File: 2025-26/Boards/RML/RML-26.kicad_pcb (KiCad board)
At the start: 2 copper layers, 90.1 x 30 mm, 26 parts, among them J1 043045-0412, Q2 AO3401A, Q3 UJ3N065080K3S, Q4 AO3401A, U1 H11L1M, U2 NE555D

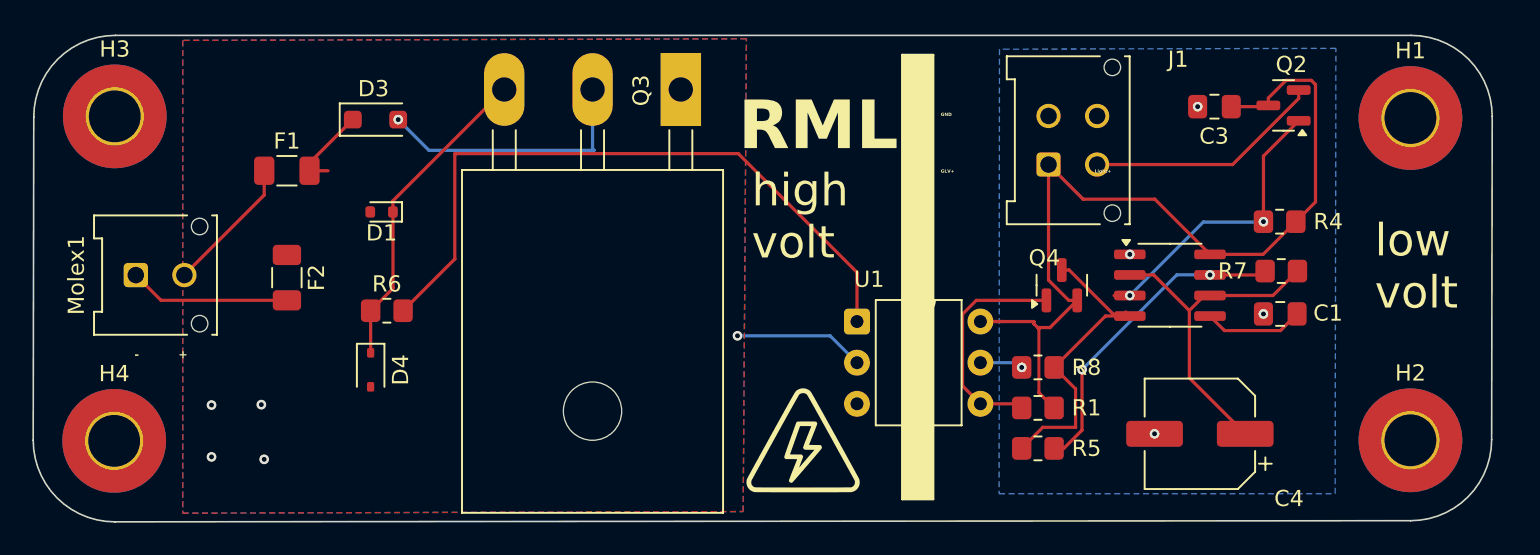
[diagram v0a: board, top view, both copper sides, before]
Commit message: fixing RML clearances
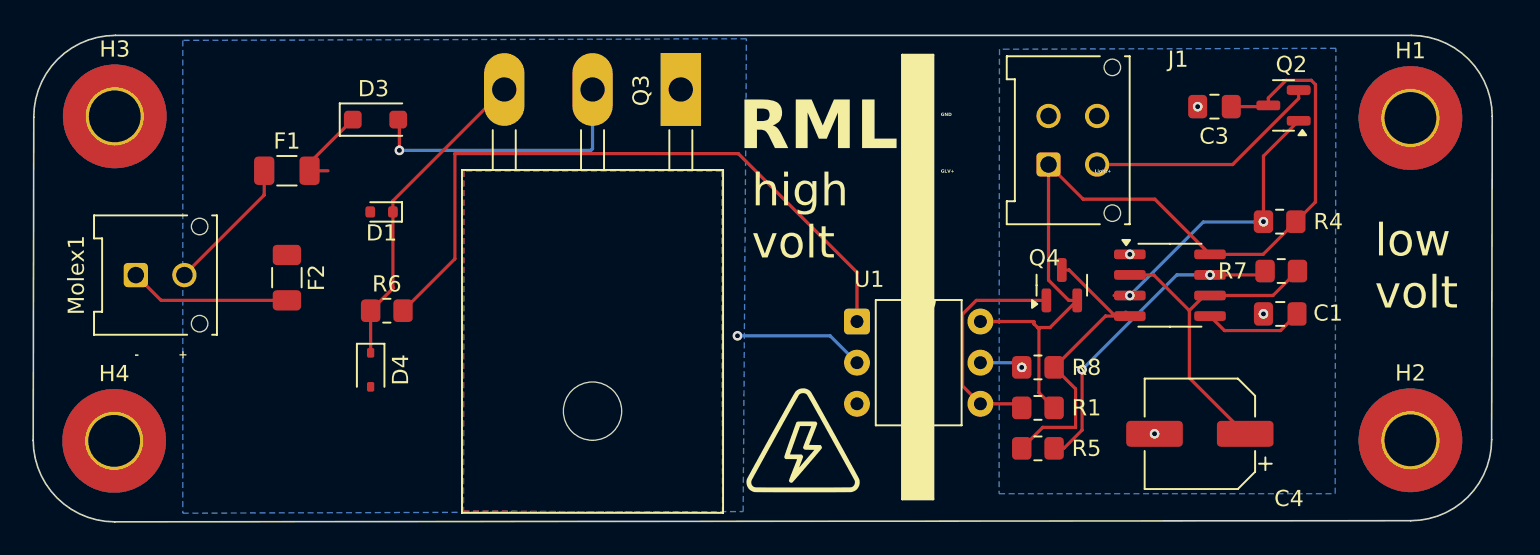
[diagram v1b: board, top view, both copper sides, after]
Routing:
- net Net-(D3-A): track 16.7 -> 17.6 mm
- net /HV-: vias 5 -> 1
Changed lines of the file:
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@@
 		)
 		(property "Value" "BZT52C51"
-			(at 0 2.1 0)
+			(at -0.025 1.975 0)
 			(layer "F.Fab")
 			(effects
@@
 		(net 2)
 	)
-	(via
-		(at 118.225 101.675)
-		(size 0.6)
-		(drill 0.3)
-		(layers "F.Cu" "B.Cu")
-		(free yes)
-		(net 2)
-	)
-	(via
-		(at 118.05 98.3)
-		(size 0.6)
-		(drill 0.3)
-		(layers "F.Cu" "B.Cu")
-		(free yes)
-		(net 2)
-	)
-	(via
-		(at 114.975 101.525)
-		(size 0.6)
-		(drill 0.3)
-		(layers "F.Cu" "B.Cu")
-		(free yes)
-		(net 2)
-	)
-	(via
-		(at 114.975 98.325)
-		(size 0.6)
-		(drill 0.3)
-		(layers "F.Cu" "B.Cu")
-		(free yes)
-		(net 2)
-	)
 	(segment
 		(start 153.1703 94.05)
@@
 		(net 3)
 	)
+	(segment
+		(start 126.575 80.775)
+		(end 126.5 80.7)
+		(width 0.2)
+		(layer "F.Cu")
+		(net 4)
+	)
+	(segment
+		(start 126.575 82.6)
+		(end 126.575 80.775)
+		(width 0.2)
+		(layer "F.Cu")
+		(net 4)
+	)
 	(via
-		(at 126.5 80.7)
+		(at 126.575 82.6)
 		(size 0.6)
 		(drill 0.3)
@@
 	)
 	(segment
-		(start 126.5 80.7)
-		(end 128.4 82.6)
-		(width 0.2)
-		(layer "B.Cu")
-		(net 4)
-	)
-	(segment
-		(start 128.4 82.6)
-		(end 138.6 82.6)
+		(start 138.4 82.6)
+		(end 138.5 82.5)
 		(width 0.2)
 		(layer "B.Cu")
@@
 	)
 	(segment
-		(start 138.6 82.6)
-		(end 138.5 82.5)
+		(start 126.575 82.6)
+		(end 138.4 82.6)
 		(width 0.2)
 		(layer "B.Cu")
@@
 		(layers "F.Cu" "B.Cu")
 		(hatch edge 0.5)
+		(priority 2)
 		(connect_pads
-			(clearance 0.5)
+			(clearance 0.762)
 		)
 		(min_thickness 0.25)
@@
 		(polygon
 			(pts
-				(xy 113.2 75.80841) (xy 113.2 105) (xy 147.8 104.9) (xy 148.002019 75.708405)
+				(xy 130.554482 83.866274) (xy 130.529482 104.866274) (xy 146.529482 104.966274) (xy 146.479482 83.866274)
 			)
 		)
@@
 			)
 		)
+	)
+	(zone
+		(net 2)
+		(net_name "/HV-")
+		(layer "B.Cu")
+		(hatch edge 0.5)
+		(connect_pads
+			(clearance 3.048)
+		)
+		(min_thickness 0.25)
+		(filled_areas_thickness no)
+		(fill yes
+			(thermal_gap 0.5)
+			(thermal_bridge_width 0.5)
+		)
+		(polygon
+			(pts
+				(xy 113.2 75.80841) (xy 113.2 105) (xy 147.8 104.9) (xy 148.002019 75.708405)
+			)
+		)

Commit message: added updated Relay, VIL, and RML
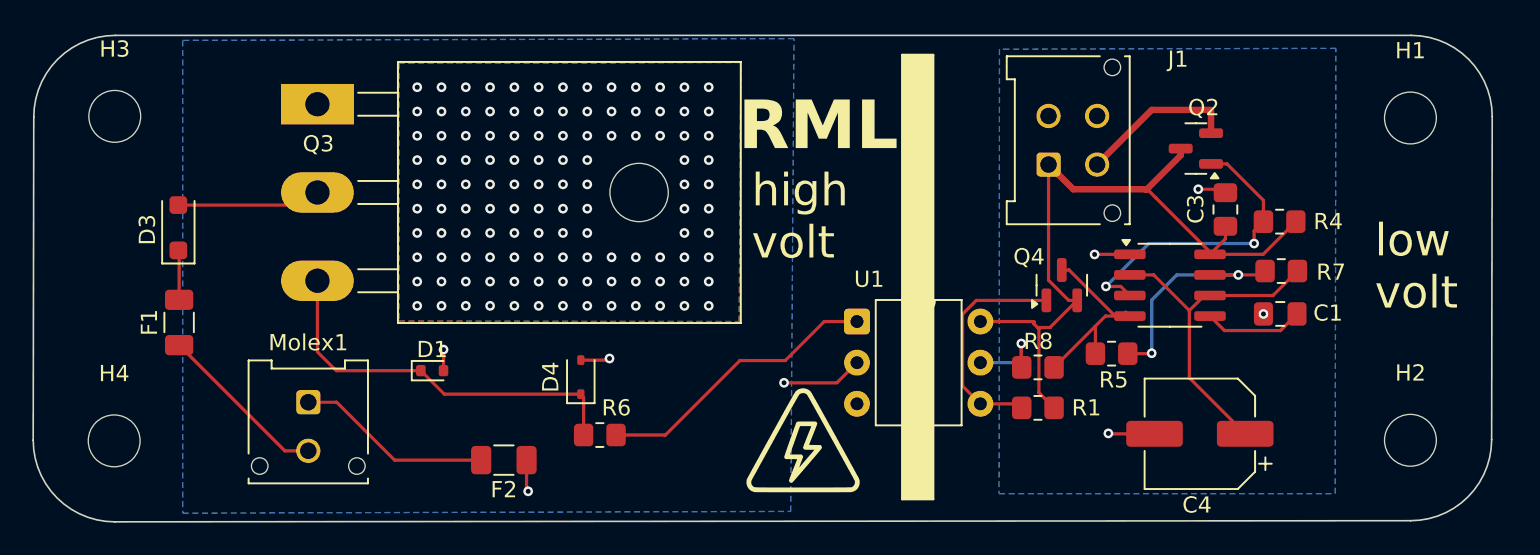
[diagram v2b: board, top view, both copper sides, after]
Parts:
- H1, H2, H3, H4: footprint MountingHole:MountingHole_3.2mm_M3_Pad_TopBottom -> MountingHole:MountingHole_3.2mm_M3
- moved Q3 22.5 mm to (121.5, 79.8), turned to -90 degrees
- moved F2 17.5 mm to (133.0, 101.7), turned to 180 degrees
- moved R6 15.2 mm to (138.9, 100.2)
- moved D3 13.9 mm to (112.9, 87.4), turned to 90 degrees
- moved Molex1 13.2 mm to (121.0, 98.2), turned to 0 degrees
- moved D4 13.0 mm to (137.8, 96.6), turned to 90 degrees
- moved F1 11.5 mm to (113.0, 93.2), turned to 90 degrees
- moved D1 10.3 mm to (128.6, 96.2), turned to 0 degrees
- moved R5 7.41 mm to (170.6, 95.2)
- moved C3 6.39 mm to (177.6, 86.2), turned to -90 degrees
- moved Q2 6.03 mm to (175.8, 82.5)
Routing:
- net Net-(R6-Pad2): track 41.9 -> 17.8 mm
- net GLV+: track 57.0 -> 45.8 mm
- net GND: track 2.67 -> 11.8 mm
- net Net-(D3-A): track 17.6 -> 8.91 mm, vias 1 -> 0
- net Net-(Q4-D): track 19.8 -> 13.4 mm
- net Net-(U2-DIS): track 19.7 -> 14.3 mm
- net Light+: track 14.7 -> 9.85 mm
- net Net-(D1-K): track 19.8 -> 24.3 mm
- net Net-(Molex1-Pin_1): track 10.1 -> 12.2 mm
- net Net-(D3-K): track 5.09 -> 3.07 mm
- net /HV-: track 8.27 -> 10.1 mm, vias 1 -> 122
- net /HV+: track 9.14 -> 10.7 mm
- net Net-(Q2-G): track 18.1 -> 19.0 mm
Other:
- board text removed: "+"
- board text removed: "-"
- board text removed: "GLV+"
- board text removed: "GND"
- board text removed: "Light+"
